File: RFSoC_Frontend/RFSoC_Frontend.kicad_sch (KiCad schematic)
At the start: 64 parts, among them J1 Conn_Coaxial, J2 Conn_Coaxial, J3 Conn_Coaxial, J4 Conn_Coaxial, J5 Conn_Coaxial, J6 Conn_Coaxial, J7 Conn_Coaxial, J8 Conn_Coaxial, U1 TCM2-33WX+, U2 TCM2-33WX+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

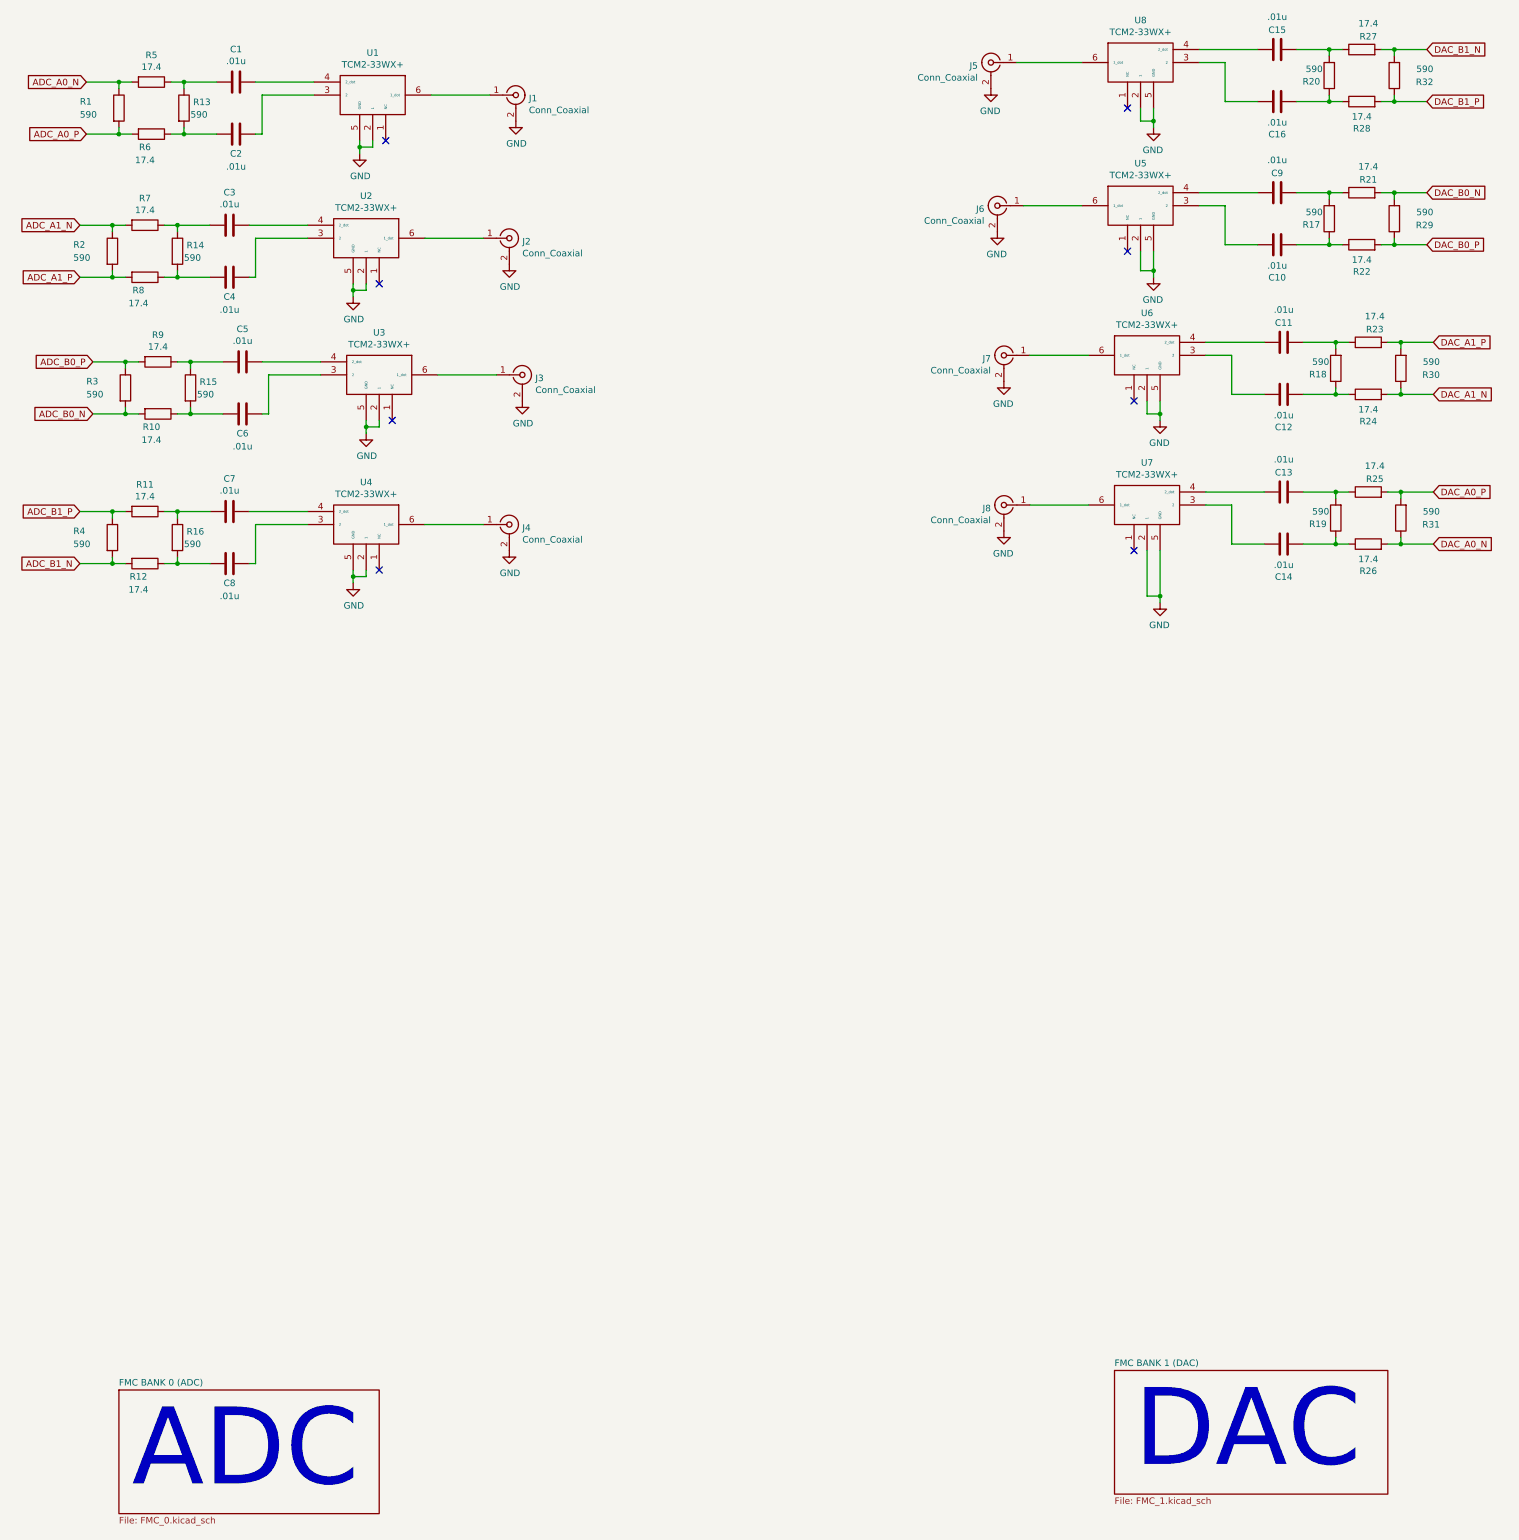
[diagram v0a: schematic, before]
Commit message: Finished Updated ADC schematic
ADC schematic was modified to match the pin map between
the rfsoc and the xm500.
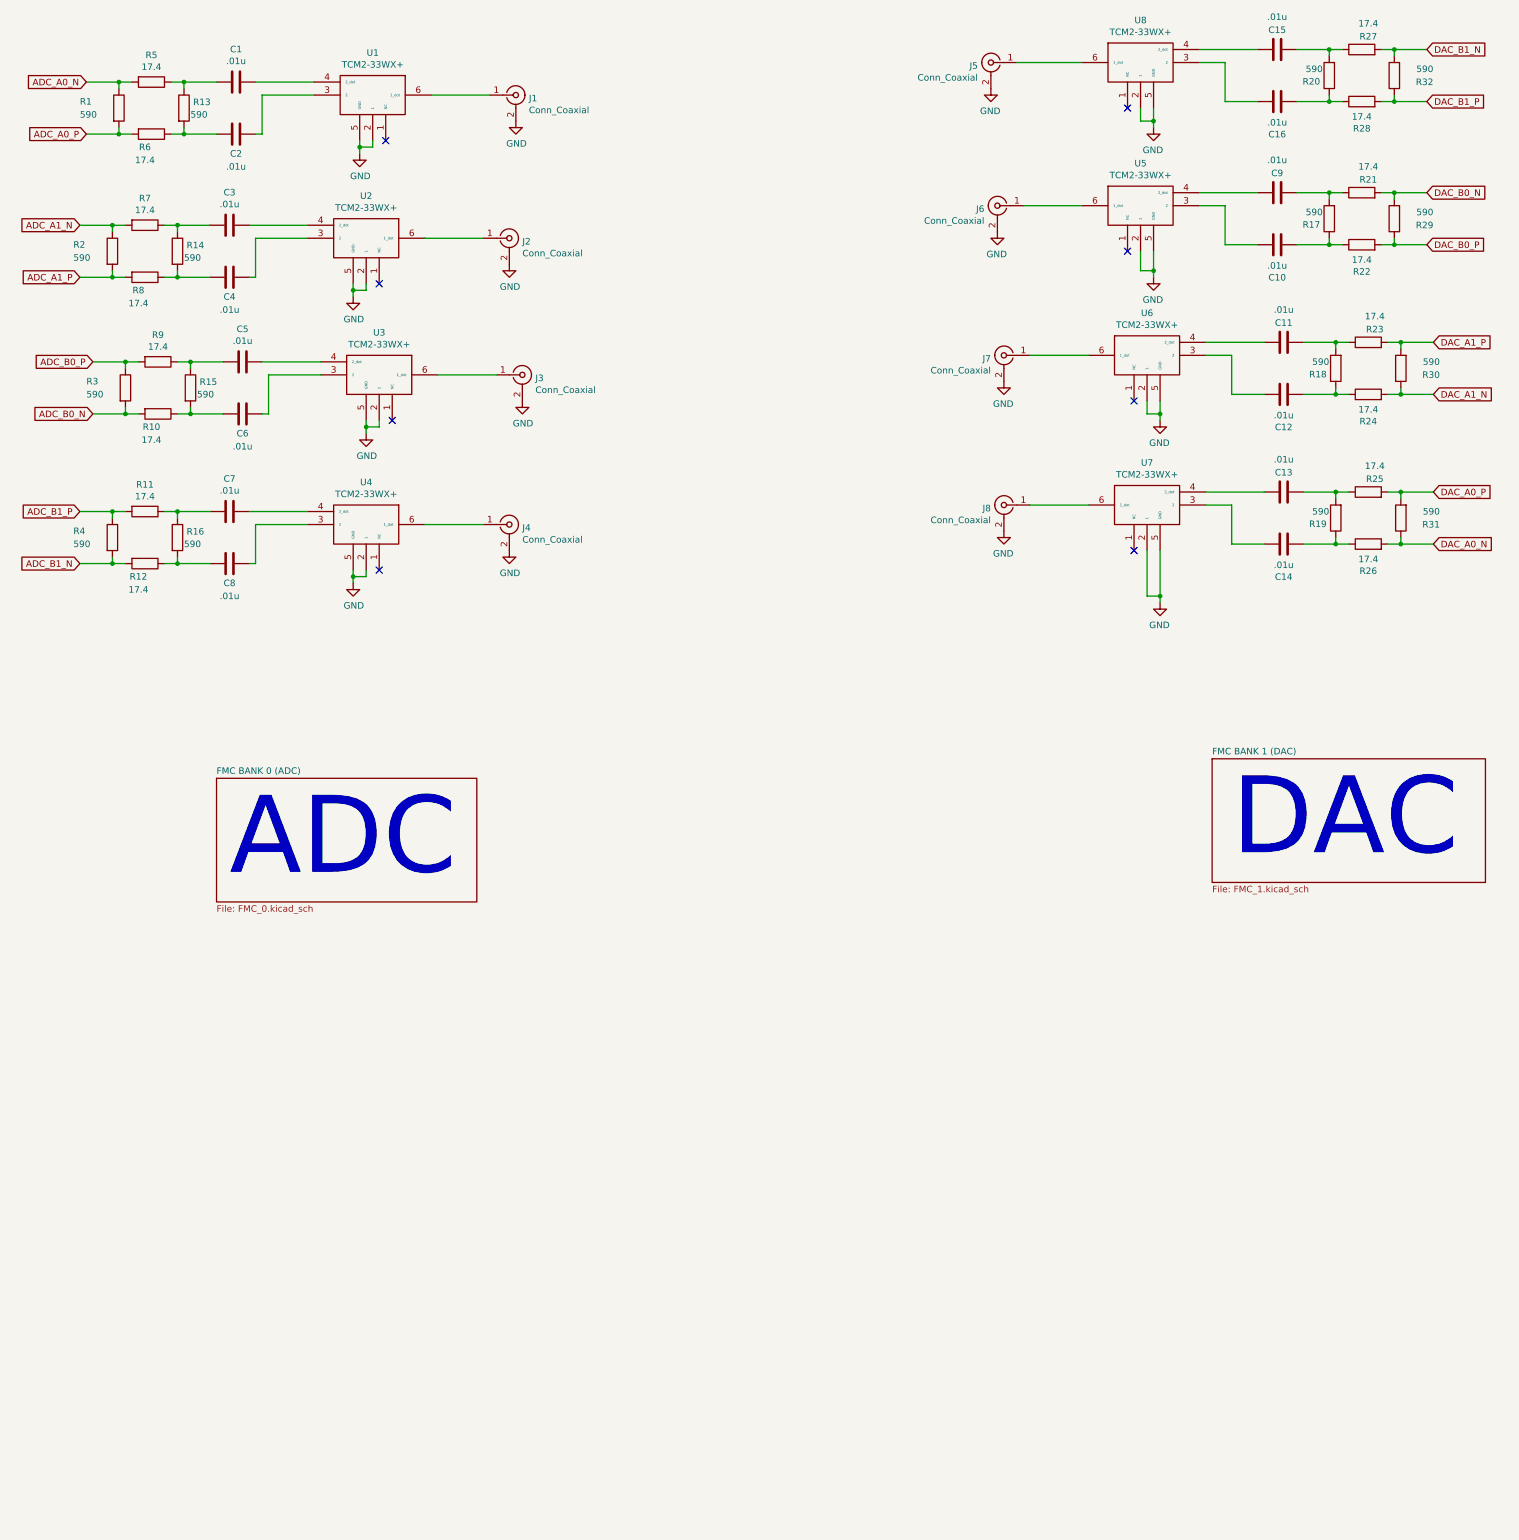
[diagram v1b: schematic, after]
